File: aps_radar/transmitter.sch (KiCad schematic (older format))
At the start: 11 parts

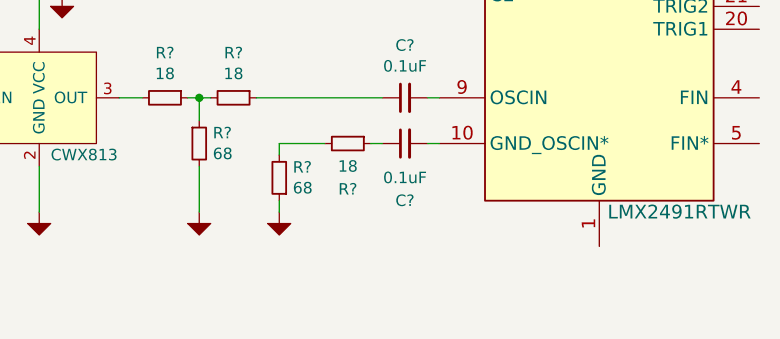
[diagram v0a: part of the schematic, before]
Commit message: Added transmitter components
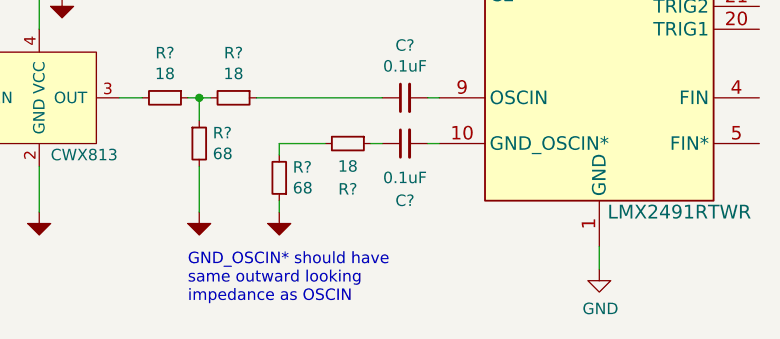
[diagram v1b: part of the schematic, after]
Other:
- note added: "GND_OSCIN* should have\nsame outward looking \nimpedance as OSCIN"
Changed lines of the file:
@@
 Wire Wire Line
 	5150 3600 5350 3600
+$Comp
+L power:GND #PWR?
+U 1 1 5E46629A
+P 6550 4150
+F 0 "#PWR?" H 6550 3900 50  0001 C CNN
+F 1 "GND" H 6555 3977 50  0000 C CNN
+F 2 "" H 6550 4150 50  0001 C CNN
+F 3 "" H 6550 4150 50  0001 C CNN
+	1    6550 4150
+	1    0    0    -1
+$EndComp
+Wire Wire Line
+	6550 4150 6550 4050
+Text Notes 4750 4300 0    50   ~ 0
+GND_OSCIN* should have\nsame outward looking \nimpedance as OSCIN
 $EndSCHEMATC

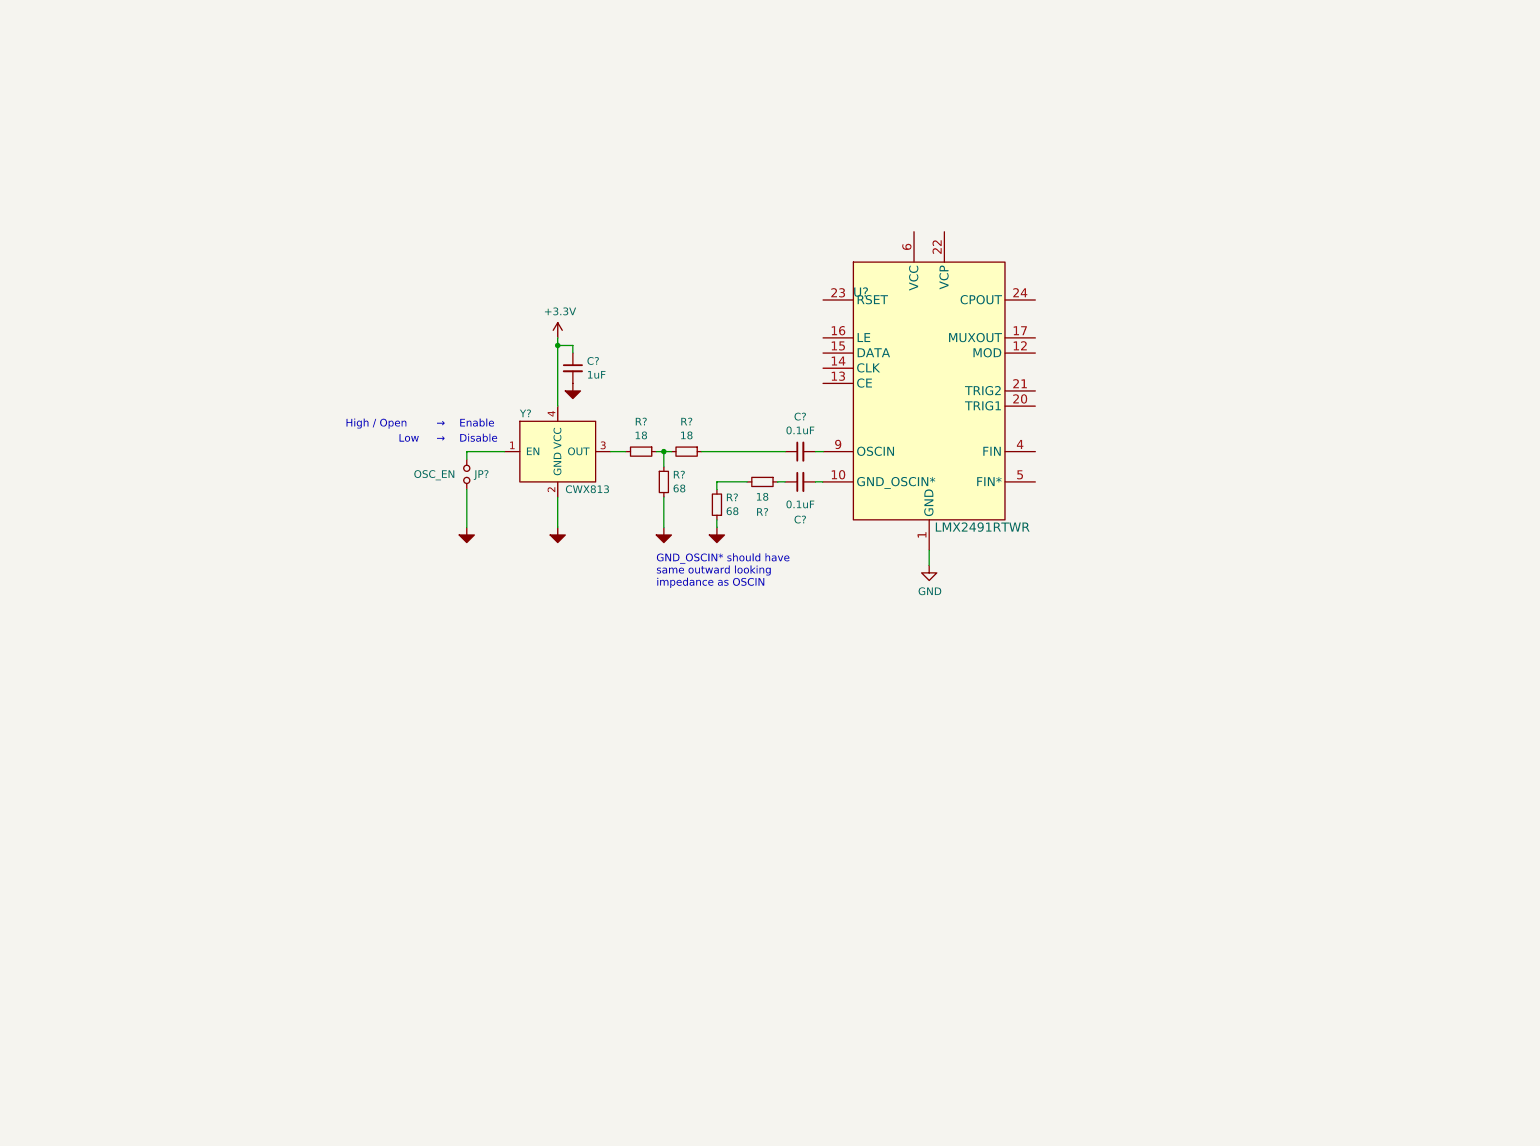
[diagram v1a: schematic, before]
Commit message: Added transmitter.sch
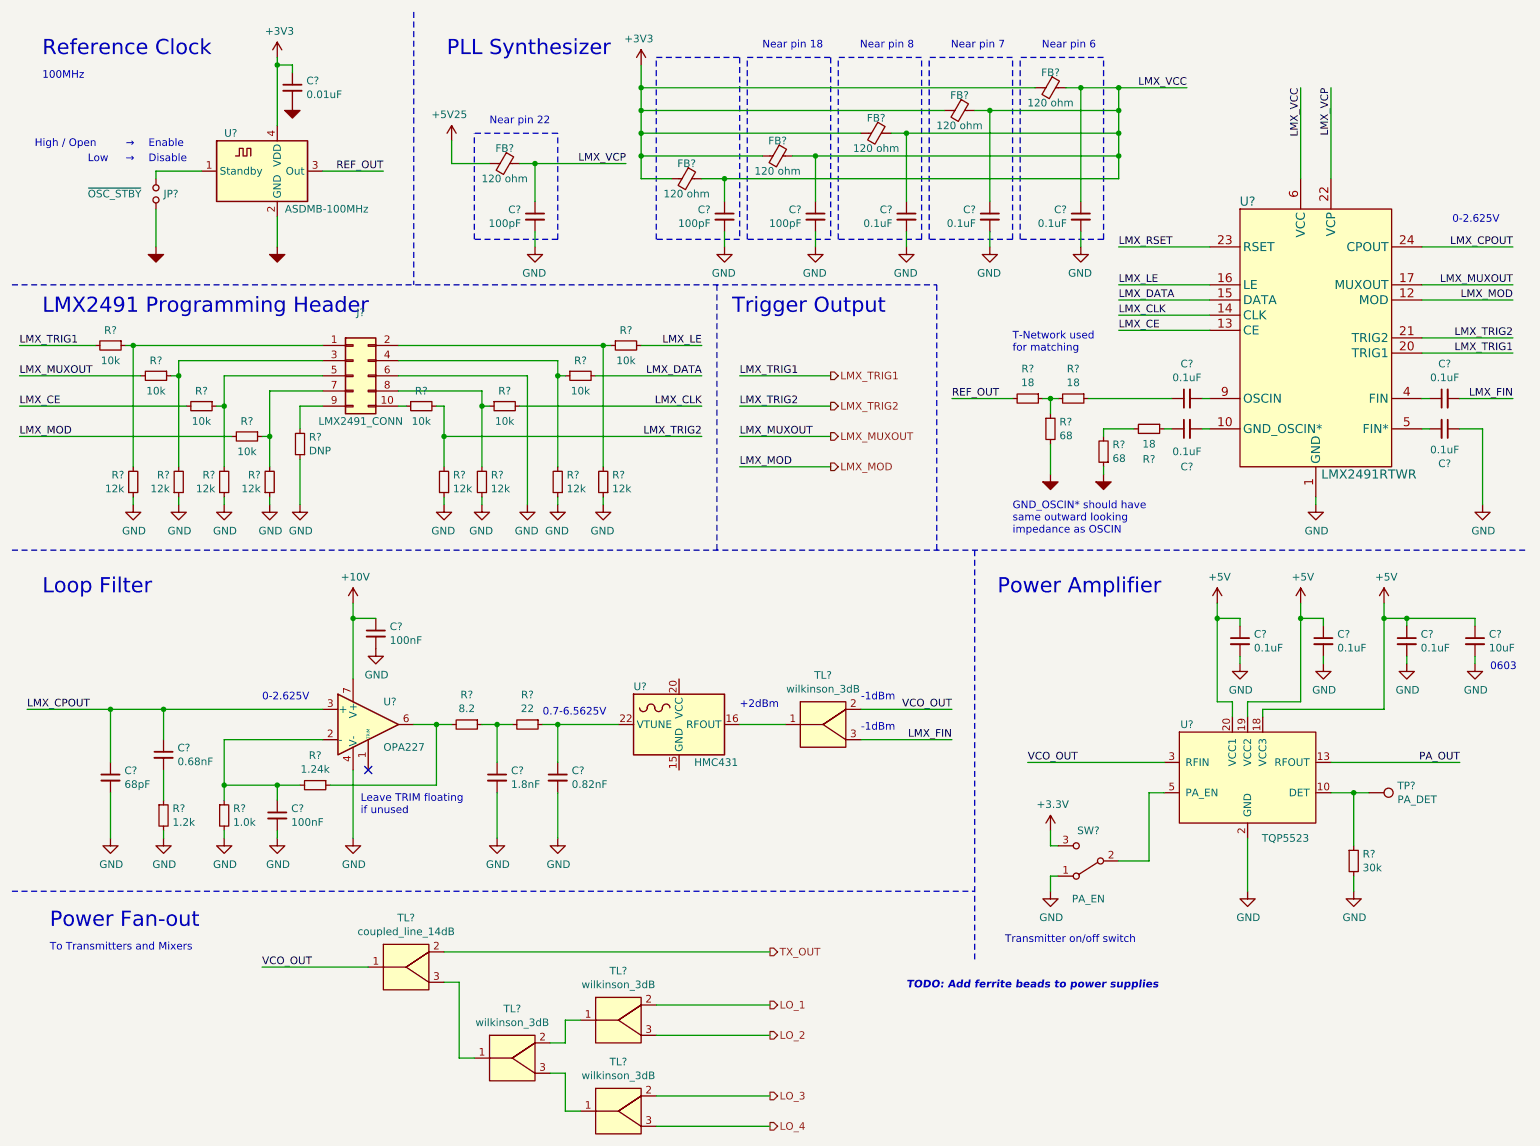
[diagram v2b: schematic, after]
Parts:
- removed Y?: CWX813, symbol aps_radar_lib:CWX813
- added C? (x8): 0.1uF, symbol Device:C_Small
- added C? (x2): 100nF, symbol Device:C_Small
- added C?: 1.8nF, symbol Device:C_Small
- added C?: 0.82nF, symbol Device:C_Small
- added C?: 0.68nF, symbol Device:C_Small
- added C?: 68pF, symbol Device:C_Small
- added C?: 10uF, symbol Device:C_Small
- added C? (x3): 100pF, symbol Device:C_Small
- added FB? (x6): 120 ohm, symbol Device:Ferrite_Bead_Small
- added J?: LMX2491_CONN, symbol Connector_Generic:Conn_02x05_Odd_Even
- added R?: 8.2, symbol Device:R_Small
- added R?: 22, symbol Device:R_Small
- added R?: 1.24k, symbol Device:R_Small
- added R?: 1.0k, symbol Device:R_Small
- added R?: 1.2k, symbol Device:R_Small
- added R?: 30k, symbol Device:R_Small
- added R? (x8): 10k, symbol Device:R_Small
- added R? (x8): 12k, symbol Device:R_Small
- added R?: DNP, symbol Device:R_Small
- added SW?: PA_EN, symbol Switch:SW_SPDT
- added TL? (x4): wilkinson_3dB, aps_radar_lib:wilkinson_3db, symbol aps_radar_lib:splitter
- added TL?: coupled_line_14dB, aps_radar_lib:coupled_line_14db, symbol aps_radar_lib:splitter
- added TP?: PA_DET, symbol Connector:TestPoint
- added U?: ASDMB-100MHz, Oscillator:Oscillator_SMD_Abracon_ASDMB-4Pin_2.5x2.0mm, symbol Oscillator:ASDMB-xxxMHz
- added U?: OPA227, Package_SO:SOIC-8_3.9x4.9mm_P1.27mm, symbol aps_radar_lib:OPA227
- added U?: HMC431, Package_DFN_QFN:QFN-24-1EP_4x4mm_P0.5mm_EP2.8x2.8mm, symbol RF:HMC431
- added U?: TQP5523, symbol aps_radar_lib:TQP5523
- C?: value 1uF -> 0.01uF
- JP?: value OSC_EN -> ~OSC_STBY
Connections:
- net +3V3: now also FB?.2, FB?.2, FB?.2, FB?.2, FB?.2, SW?.3 (C), U?.4 (VDD)
- net GND: now also C?.1, C?.2, C?.2, C?.2, C?.2, C?.2, C?.2, C?.2, C?.2, C?.2, C?.2, C?.2, C?.2, C?.2, C?.2, C?.2, J?.6 (Pin_6), R?.1, R?.1, R?.1, R?.1, R?.1, R?.1, R?.1, R?.1, R?.1, R?.2, R?.2, R?.2, SW?.1 (A), U?.11 (GND), U?.12 (GND), U?.14 (GND), U?.15 (GND), U?.16 (GND), U?.17 (GND), U?.2 (GND), U?.21 (GND_PAD), U?.4 (GND), U?.4 (V-)
- net VCC: now also C?.1, C?.1, C?.1, C?.1, C?.1, FB?.1, FB?.1, FB?.1, FB?.1, FB?.1
- net at JP?.2: now also U?.1 (Standby)
- net REF_OUT: now reaches R?.2
- net REF_OUT: now also U?.3 (Out)
- net LMX_MOD: now reaches U?.12 (MOD)
- net LMX_MOD: now also R?.2
- net LMX_CE: now reaches U?.13 (CE)
- net LMX_CE: now also R?.2
- net LMX_CLK: now reaches U?.14 (CLK)
- net LMX_CLK: now also R?.2
- net LMX_DATA: now reaches U?.15 (DATA)
- net LMX_DATA: now also R?.2
- net LMX_LE: now reaches U?.16 (LE)
- net LMX_LE: now also R?.2
- net LMX_MUXOUT: now reaches U?.17 (MUXOUT)
- net LMX_MUXOUT: now also R?.2
- net LMX_TRIG1: now reaches U?.20 (TRIG1)
- net LMX_TRIG1: now also R?.2
- net LMX_TRIG2: now reaches U?.21 (TRIG2)
- net LMX_TRIG2: now also R?.2, R?.2
- net LMX_VCP: now reaches U?.22 (VCP)
- net LMX_VCP: now also C?.1, FB?.1
- net LMX_RSET: now reaches U?.23 (RSET)
- net LMX_CPOUT: now reaches U?.24 (CPOUT)
- net LMX_CPOUT: now also C?.1, C?.1, U?.3 (+)
- net at U?.4 (FIN): now also C?.1
- net at U?.5 (FIN*): now also C?.2
- new net: U?.1 (TRIM), U?.8 (TRIM)
- new net: C?.1, R?.1, R?.2, U?.2 (-)
- new net: R?.1, R?.2, U?.6
- new net: TL?.1, TL?.3 (x2)
- new net: TL?.1, TL?.2
- new net: U?.15 (GND), U?.25 (GND)
- new net: TL?.1, U?.16 (RFOUT)
- new net: C?.1, R?.1, U?.22 (VTUNE)
- new net: C?.1, R?.1, R?.2
- new net: C?.2, R?.1
- new net: U?.1 (NC), U?.6 (NC), U?.7 (NC), U?.8 (NC), U?.9 (NC)
- new net: R?.1, TP?.1, U?.10 (DET)
- new net: SW?.2 (B), U?.5 (PA_EN)
- new net: J?.1 (Pin_1), R?.1, R?.2
- new net: J?.10 (Pin_10), R?.1
- new net: J?.2 (Pin_2), R?.1, R?.2
- new net: J?.3 (Pin_3), R?.1, R?.2
- new net: J?.4 (Pin_4), R?.1, R?.2
- new net: J?.5 (Pin_5), R?.1, R?.2
- new net: J?.7 (Pin_7), R?.1, R?.2
- new net: J?.8 (Pin_8), R?.1, R?.2
- new net: J?.9 (Pin_9), R?.2
- new net +10V: C?.1, U?.7 (V+)
- new net +5V: C?.1, C?.1, C?.1, C?.1, FB?.2, U?.18 (VCC3), U?.19 (VCC2), U?.20 (VCC1)
- new net LMX_FIN: C?.2, TL?.3
- new net LO_1: TL?.2
- new net LO_2: TL?.3
- new net LO_3: TL?.2
- new net LO_4: TL?.3
- new net PA_OUT: U?.13 (RFOUT)
- new net TX_OUT: TL?.2
- new net VCO_OUT: TL?.1, TL?.2, U?.3 (RFIN)
- no-connect marks 0 -> 1
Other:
- note added: "+2dBm"
- note added: "-1dBm"
- note added: "0-2.625V"
- note added: "0.7-6.5625V"
- note added: "0603"
- note added: "100MHz"
- note added: "LMX2491 Programming Header"
- note added: "Leave TRIM floating\nif unused"
- note added: "Loop Filter"
- note added: "Near pin 18"
- note added: "Near pin 22"
- note added: "Near pin 6"
- note added: "Near pin 7"
- note added: "Near pin 8"
- note added: "PLL Synthesizer"
- note added: "Power Amplifier"
- note added: "Power Fan-out"
- note added: "Reference Clock"
- note added: "T-Network used\nfor matching"
- note added: "TODO: Add ferrite beads to power supplies"
- note added: "To Transmitters and Mixers"
- note added: "Transmitter on/off switch"
- note added: "Trigger Output"
- moved on the sheet: C?, JP?, R?, U?
